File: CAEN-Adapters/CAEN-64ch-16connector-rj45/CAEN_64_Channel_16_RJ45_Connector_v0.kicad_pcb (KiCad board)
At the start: 2 copper layers, 115 x 90 mm, 18 parts

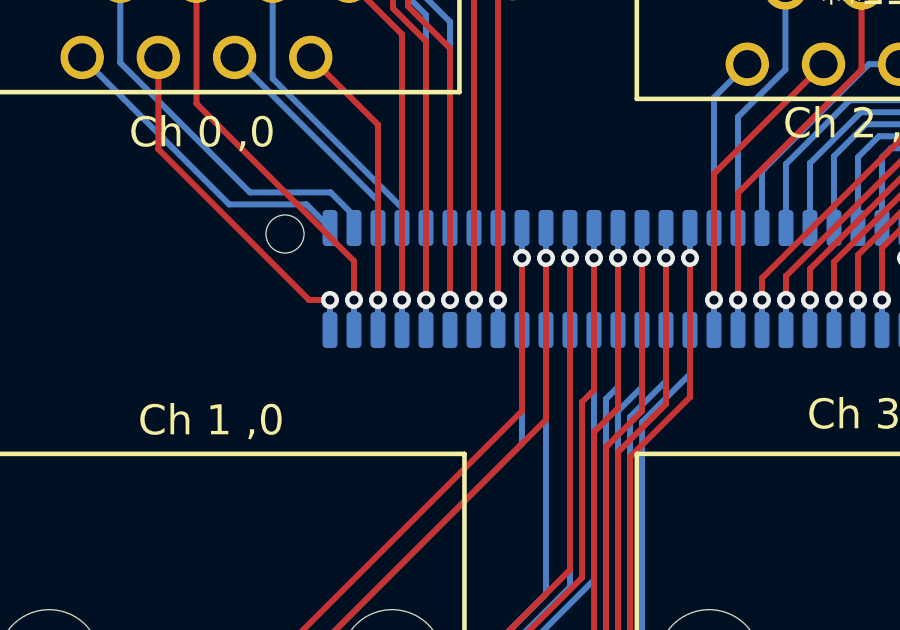
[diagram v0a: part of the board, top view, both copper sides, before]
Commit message: Corrected channel 5 connection
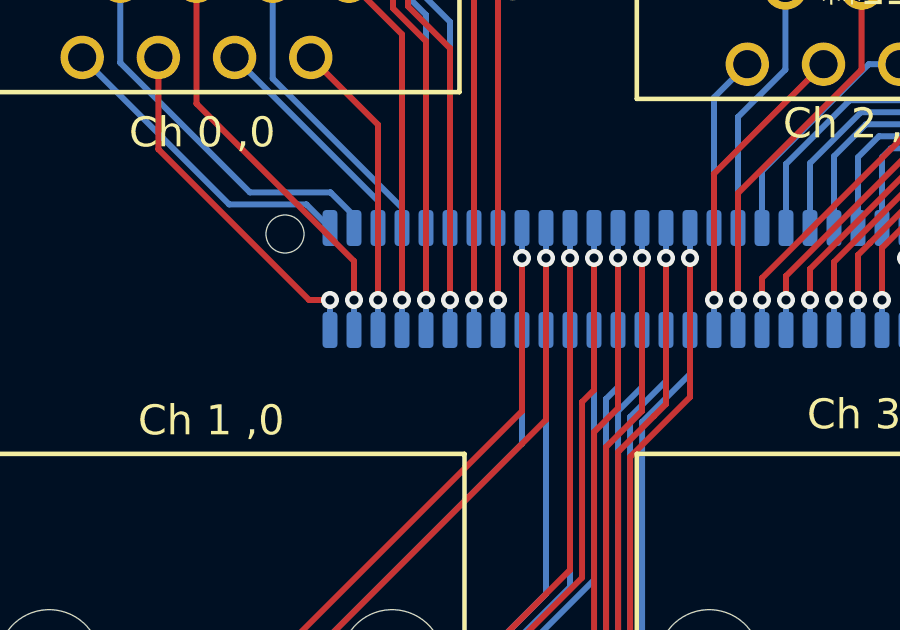
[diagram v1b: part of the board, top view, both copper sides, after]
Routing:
- net c5: track 31.3 -> 32.3 mm
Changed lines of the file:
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@@
+	)
+	(segment
+		(start 123.2 107.4)
+		(end 123.2 106.4)
+		(width 0.2)
+		(layer "B.Cu")
+		(net 70)
 	)
 	(segment
